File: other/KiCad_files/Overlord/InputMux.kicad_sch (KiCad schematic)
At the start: 18 parts, among them IC1 74HC4052D,653

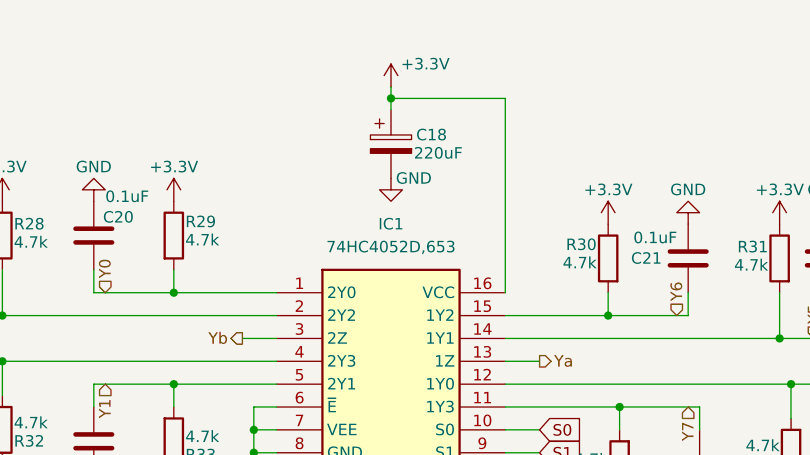
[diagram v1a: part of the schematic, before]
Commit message: Sent for PCB production, ver 2.1 rev A
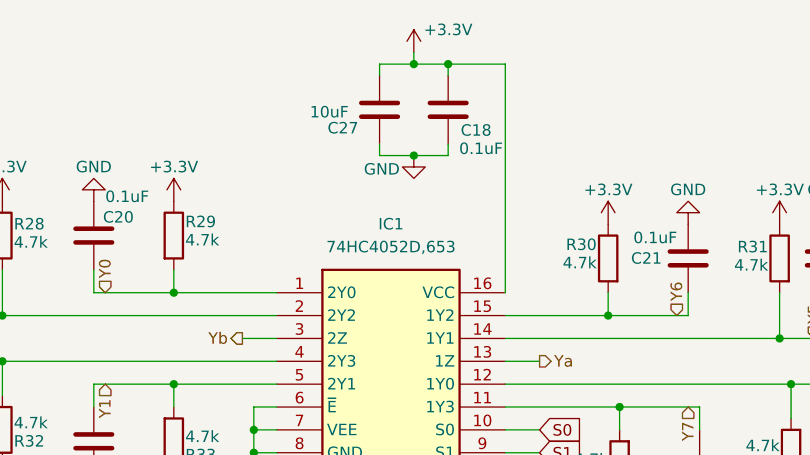
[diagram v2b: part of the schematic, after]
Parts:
- removed C18: 220uF, Capacitor_THT:CP_Radial_D8.0mm_P3.50mm, symbol Device:C_Polarized
- added C18: 0.1uF, Capacitor_SMD:C_0805_2012Metric_Pad1.18x1.45mm_HandSolder, symbol Device:C
- added C27: 10uF, Capacitor_SMD:C_0805_2012Metric_Pad1.18x1.45mm_HandSolder, symbol Device:C
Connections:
- net +3.3V: now also C18.2, C27.2
- net GND: now also C18.1, C27.1

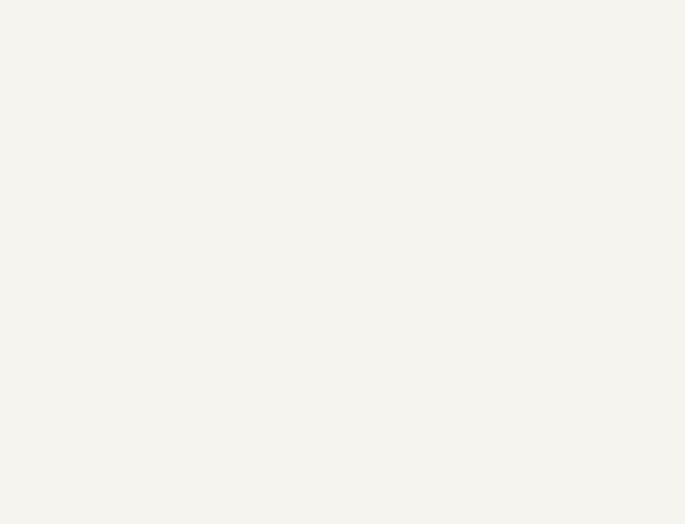
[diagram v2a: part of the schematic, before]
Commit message: Fixed PCB - changed modbus H/L to A/B - changed RS485 IC to a cheaper variant, fixed pullup resistors - added pullup on boot pin GPIO0 - removed unused power supplies and rerouted USB+5V for better voltage control - added transient voltage suppresion on digital inputs
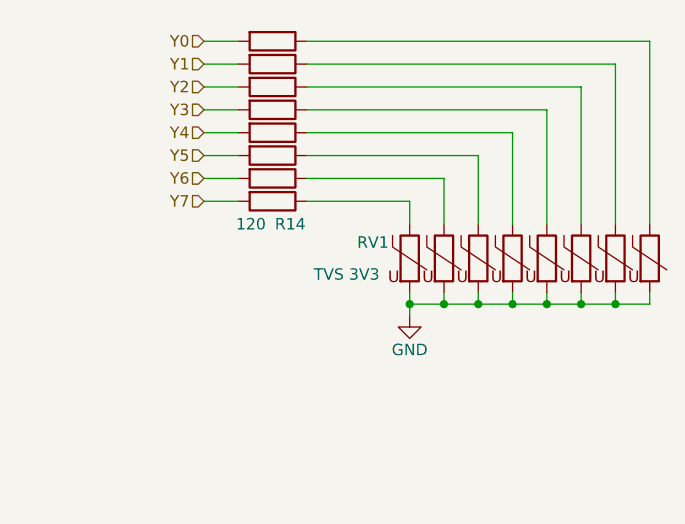
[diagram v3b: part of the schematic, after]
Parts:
- added R14, R61, R65, R69, R73, R77, R81, R85: 120, Resistor_SMD:R_0805_2012Metric_Pad1.20x1.40mm_HandSolder, symbol Device:R
- added RV1, RV13, RV14, RV21, RV22, RV23, RV5, RV9: TVS 3V3, Resistor_SMD:R_0805_2012Metric_Pad1.20x1.40mm_HandSolder, symbol Device:Varistor
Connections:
- net GND: now also RV1.2, RV13.2, RV14.2, RV21.2, RV22.2, RV23.2, RV5.2, RV9.2
- net Y0: now also R85.2
- net Y1: now also R81.2
- net Y2: now also R77.2
- net Y3: now also R73.2
- net Y4: now also R69.2
- net Y5: now also R65.2
- net Y6: now also R61.2
- net Y7: now also R14.2
- new net: R73.1, RV14.1
- new net: R81.1, RV22.1
- new net: R14.1, RV1.1
- new net: R61.1, RV5.1
- new net: R65.1, RV9.1
- new net: R77.1, RV21.1
- new net: R69.1, RV13.1
- new net: R85.1, RV23.1
